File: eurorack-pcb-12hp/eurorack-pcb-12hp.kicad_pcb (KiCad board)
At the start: 2 copper layers, 79.4 x 108.3 mm, 0 parts

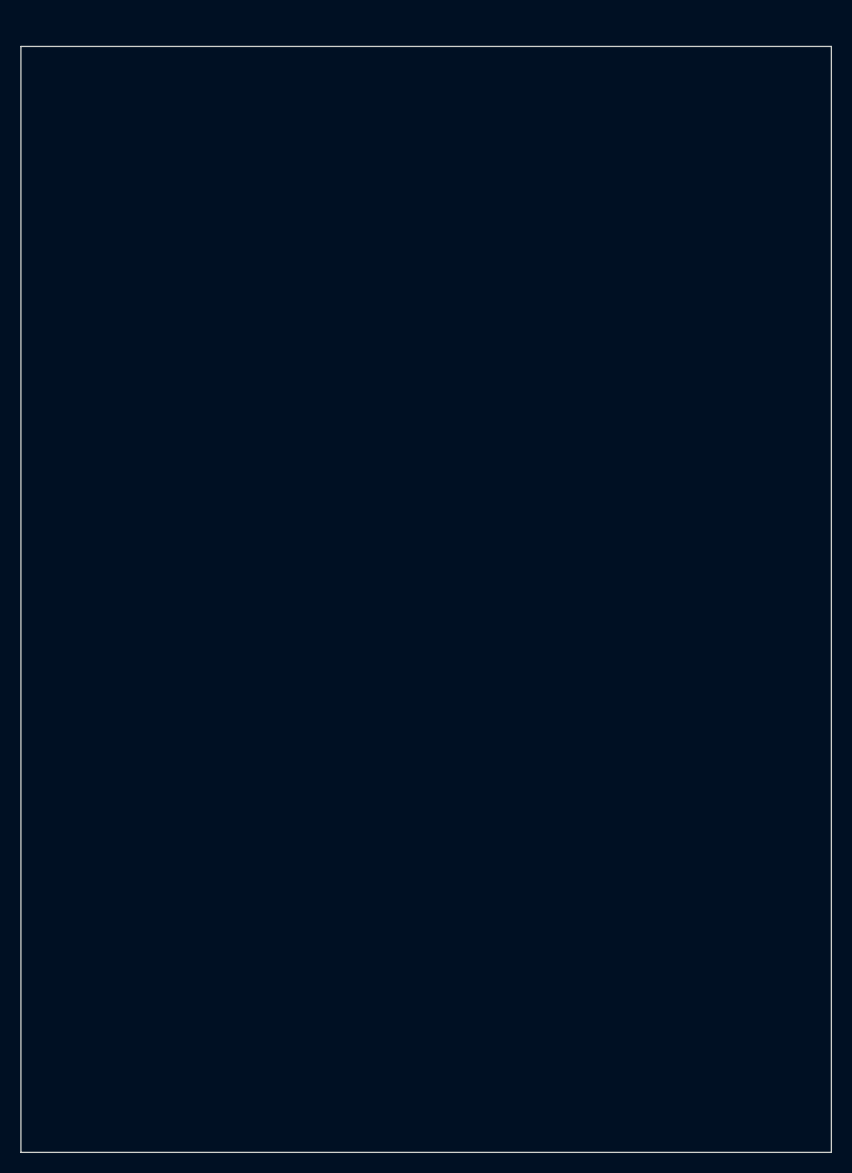
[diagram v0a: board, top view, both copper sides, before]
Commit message: Minor adjustments to PCB positioning. Moving everything into a single folder to be easier for kiCad to pick up all templates from user-template path
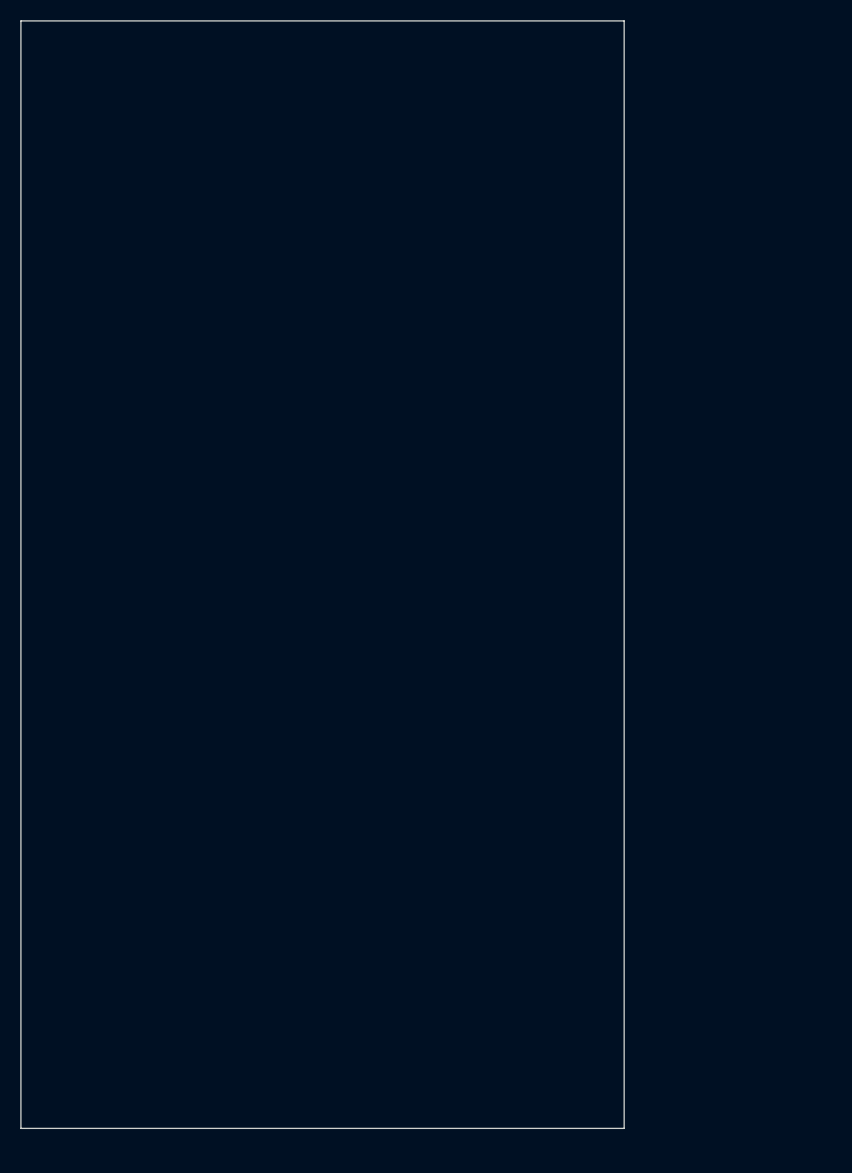
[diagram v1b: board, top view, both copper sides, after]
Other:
- board size 79.4 x 108.3 mm -> 59.1 x 108.5 mm
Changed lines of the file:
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@@
   )
   (net 0 "")
-  (gr_line (start 0.75 12.5) (end 0.75 120.85) (layer "Edge.Cuts") (width 0.1))
-  (gr_line (start 80.15 120.85) (end 80.15 12.5) (layer "Edge.Cuts") (width 0.1))
-  (gr_line (start 0.75 120.85) (end 80.15 120.85) (layer "Edge.Cuts") (width 0.1))
-  (gr_line (start 0.75 12.5) (end 80.15 12.5) (layer "Edge.Cuts") (width 0.1))
-  (gr_line (start 80.9 0) (end 80.9 128.5) (layer "User.1") (width 0.1))
+  (gr_line (start 0.75 10) (end 0.75 118.5) (layer "Edge.Cuts") (width 0.1))
+  (gr_line (start 59.85 118.5) (end 59.85 10) (layer "Edge.Cuts") (width 0.1))
+  (gr_line (start 0.75 118.5) (end 59.85 118.5) (layer "Edge.Cuts") (width 0.1))
+  (gr_line (start 0.75 10) (end 59.85 10) (layer "Edge.Cuts") (width 0.1))
+  (gr_line (start 60.6 0) (end 60.6 128.5) (layer "User.1") (width 0.1))
   (gr_line (start 0 128.5) (end 0 0) (layer "User.1") (width 0.1))
-  (gr_line (start 0 0) (end 80.9 0) (layer "User.1") (width 0.1))
-  (gr_line (start 80.9 128.5) (end 0 128.5) (layer "User.1") (width 0.1))
+  (gr_line (start 0 0) (end 60.6 0) (layer "User.1") (width 0.1))
+  (gr_line (start 60.6 128.5) (end 0 128.5) (layer "User.1") (width 0.1))
 )
